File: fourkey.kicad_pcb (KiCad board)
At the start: 2 copper layers, 85.3 x 77.7 mm, 23 parts, among them K1 KEYSW, K2 KEYSW, K3 KEYSW, K4 KEYSW, SW1 RESET, U1 ProMicro

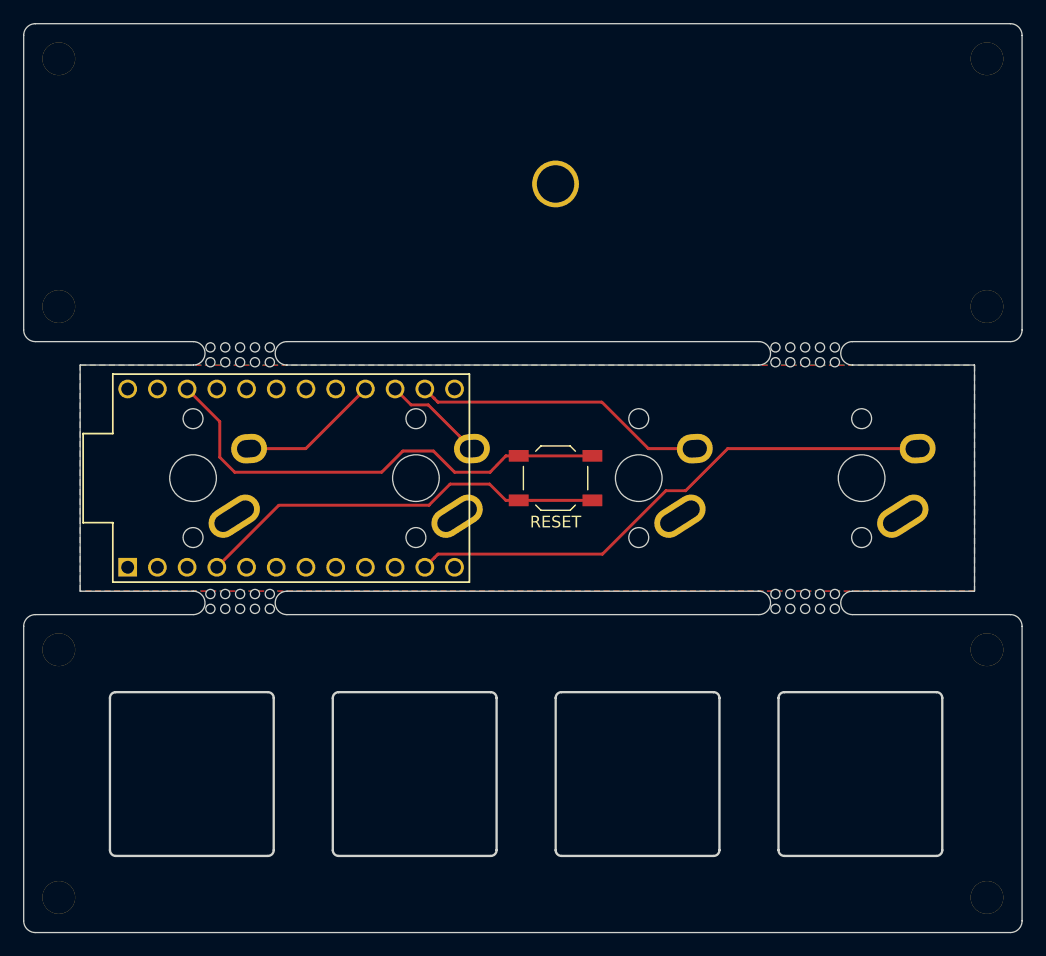
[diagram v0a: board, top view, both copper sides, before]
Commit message: change mounting holes to m2
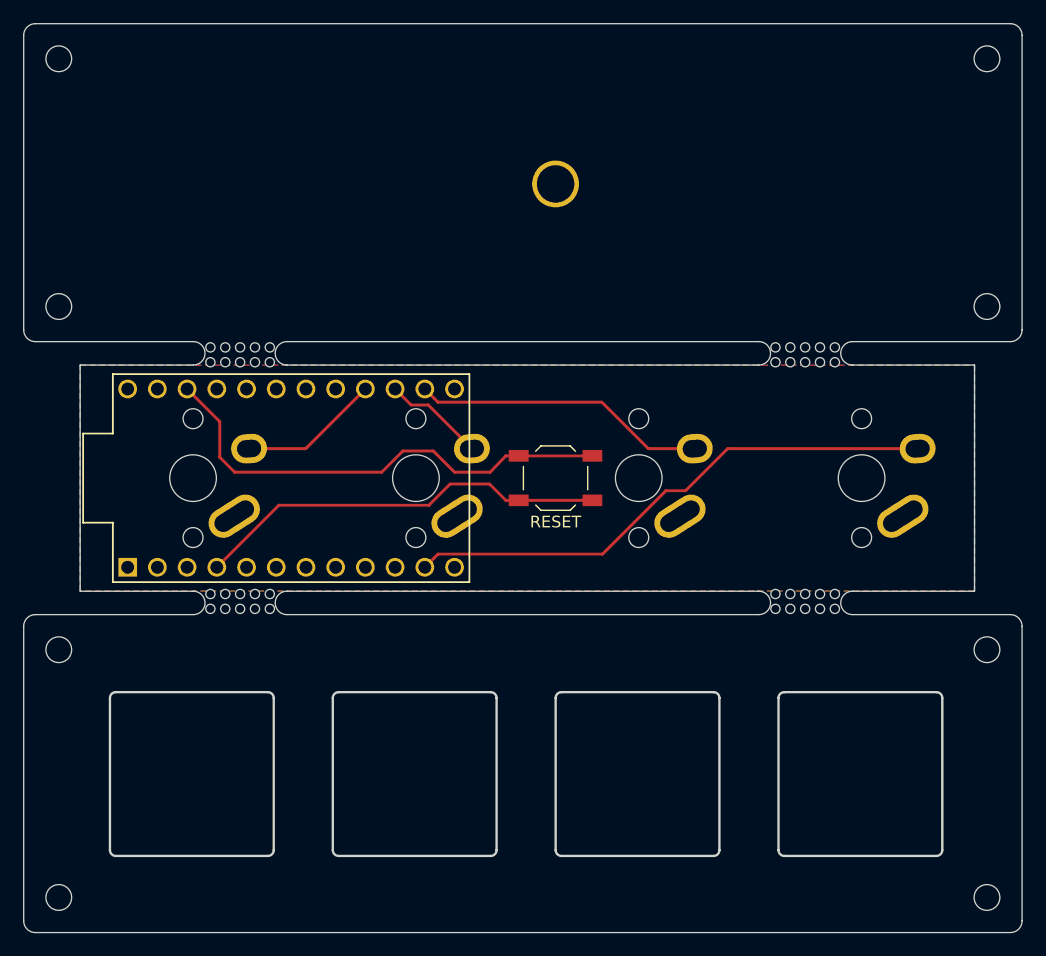
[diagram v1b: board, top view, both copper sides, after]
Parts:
- HOLE_M2.6 (x8): footprint keyboard_parts:HOLE_M2.6 -> MountingHole:MountingHole_2.2mm_M2_DIN965

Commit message: add extra screw holes
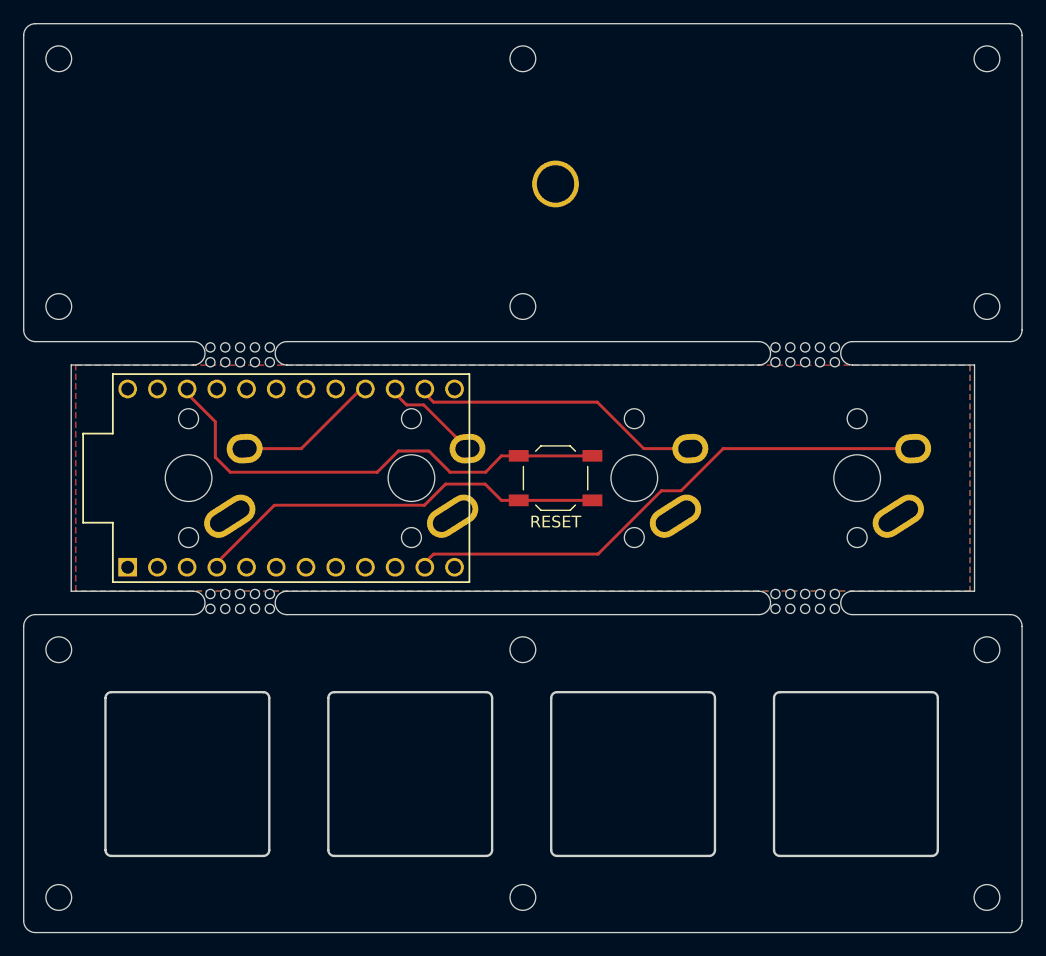
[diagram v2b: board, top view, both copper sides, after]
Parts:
- added HOLE_M2.6: VAL**, MountingHole:MountingHole_2.2mm_M2_DIN965, F.Cu at (106.2, 94.2)
- added HOLE_M2.6: VAL**, MountingHole:MountingHole_2.2mm_M2_DIN965, F.Cu at (106.2, 115.3)
- added HOLE_M2.6: VAL**, MountingHole:MountingHole_2.2mm_M2_DIN965, F.Cu at (106.2, 43.7)
- added HOLE_M2.6: VAL**, MountingHole:MountingHole_2.2mm_M2_DIN965, F.Cu at (106.2, 64.8)
- moved K1 0.38 mm to (77.6, 79.5)
- moved K2 0.38 mm to (96.6, 79.5)
- moved K3 0.38 mm to (115.7, 79.5)
- moved K4 0.38 mm to (134.7, 79.5)
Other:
- outline, holes or cut-outs redrawn

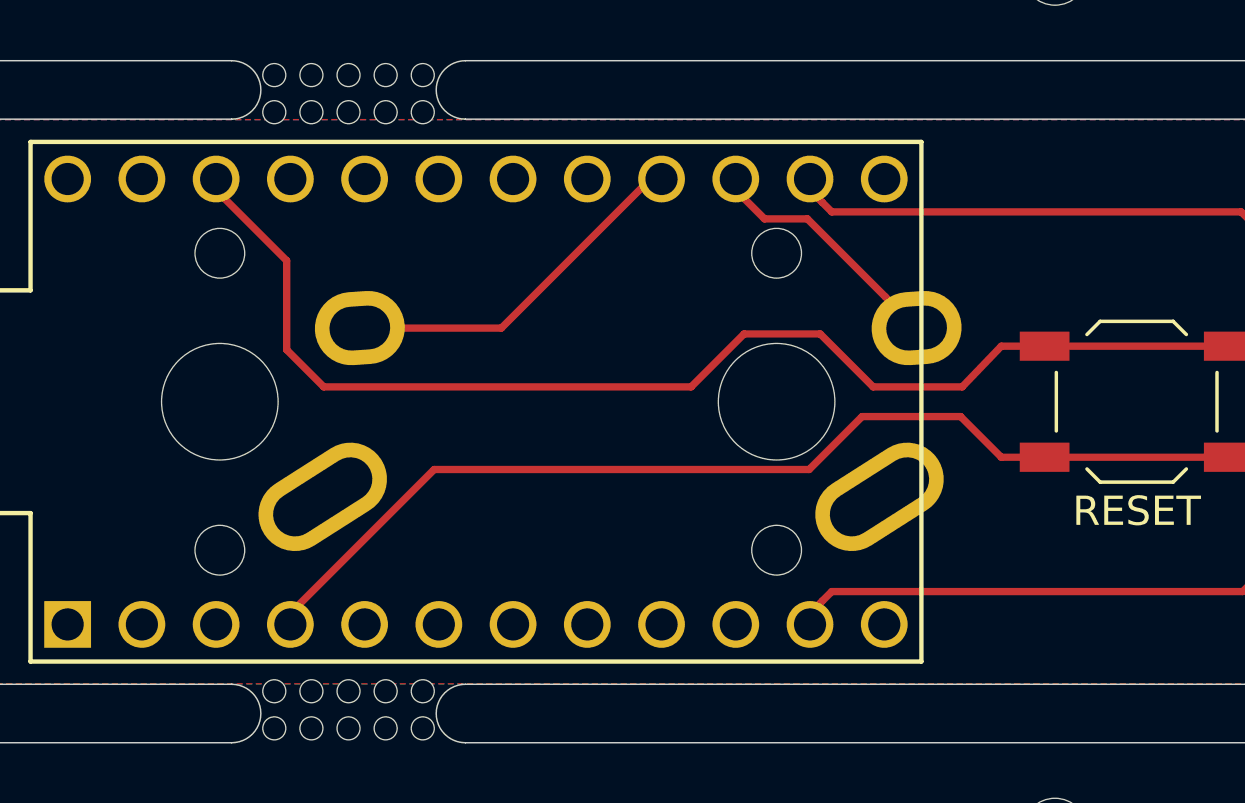
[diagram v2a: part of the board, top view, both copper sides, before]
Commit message: some trace rerouting
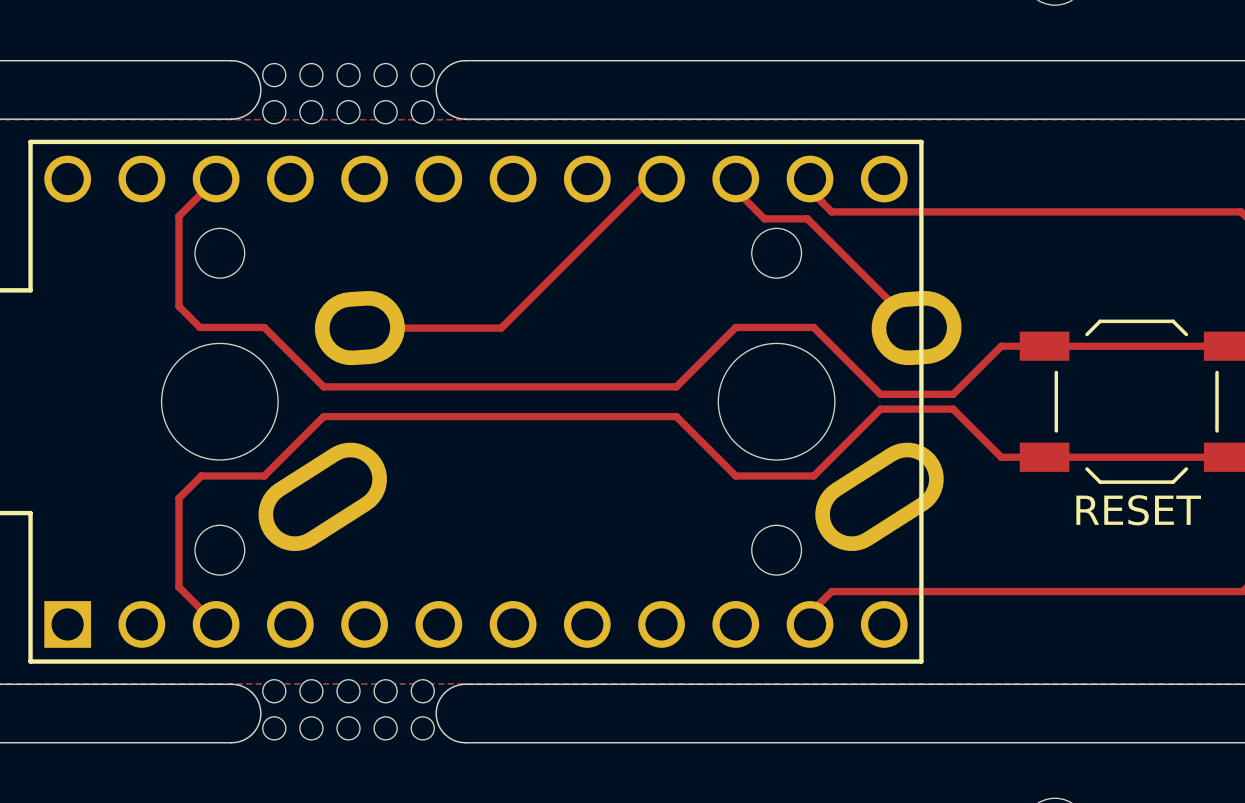
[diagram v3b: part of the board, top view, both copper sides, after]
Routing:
- net +5V: track 35.6 -> 44.0 mm
- net /Reset: track 41.5 -> 44.0 mm
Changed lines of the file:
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@@
     (thickness 1.6)
     (drawings 69)
-    (tracks 38)
+    (tracks 45)
     (zones 0)
     (modules 27)
@@
   (layers
     (0 F.Cu signal)
-    (31 B.Cu signal)
+    (31 B.Cu signal hide)
     (32 B.Adhes user)
     (33 F.Adhes user)
@@
     (38 B.Mask user)
     (39 F.Mask user)
-    (40 Dwgs.User user)
+    (40 Dwgs.User user hide)
     (41 Cmts.User user)
     (42 Eco1.User user)
@@
   (segment (start 139.537 76.982) (end 123.297 76.982) (width 0.25) (layer F.Cu) (net 7))
   (segment (start 105.435 77.602) (end 111.735 77.602) (width 0.25) (layer F.Cu) (net 9))
-  (segment (start 102.997 78.994) (end 104.335 77.602) (width 0.25) (layer F.Cu) (net 9))
   (segment (start 104.335 77.602) (end 105.435 77.602) (width 0.25) (layer F.Cu) (net 9))
-  (segment (start 98.138099 77.183099) (end 99.949 78.994) (width 0.25) (layer F.Cu) (net 9))
-  (segment (start 77.089 71.882) (end 79.883 74.676) (width 0.25) (layer F.Cu) (net 9))
-  (segment (start 93.723026 78.994) (end 95.533927 77.183099) (width 0.25) (layer F.Cu) (net 9))
-  (segment (start 81.153 78.994) (end 93.723026 78.994) (width 0.25) (layer F.Cu) (net 9))
-  (segment (start 79.883 77.724) (end 81.153 78.994) (width 0.25) (layer F.Cu) (net 9))
-  (segment (start 99.949 78.994) (end 102.997 78.994) (width 0.25) (layer F.Cu) (net 9))
-  (segment (start 95.533927 77.183099) (end 98.138099 77.183099) (width 0.25) (layer F.Cu) (net 9))
-  (segment (start 79.883 74.676) (end 79.883 77.724) (width 0.25) (layer F.Cu) (net 9))
-  (segment (start 104.335 81.402) (end 102.943 80.01) (width 0.25) (layer F.Cu) (net 10))
-  (segment (start 105.435 81.402) (end 104.335 81.402) (width 0.25) (layer F.Cu) (net 10))
-  (segment (start 102.943 80.01) (end 99.570974 80.01) (width 0.25) (layer F.Cu) (net 10))
+  (segment (start 100.203 79.248) (end 102.689 79.248) (width 0.25) (layer F.Cu) (net 9))
+  (segment (start 76.917333 76.962) (end 79.121 76.962) (width 0.25) (layer F.Cu) (net 9))
+  (segment (start 97.917 76.962) (end 100.203 79.248) (width 0.25) (layer F.Cu) (net 9))
+  (segment (start 95.25 76.962) (end 97.917 76.962) (width 0.25) (layer F.Cu) (net 9))
+  (segment (start 93.218 78.994) (end 95.25 76.962) (width 0.25) (layer F.Cu) (net 9))
+  (segment (start 77.47 71.882) (end 76.2 73.152) (width 0.25) (layer F.Cu) (net 9))
+  (segment (start 79.121 76.962) (end 81.153 78.994) (width 0.25) (layer F.Cu) (net 9))
+  (segment (start 81.153 78.994) (end 93.218 78.994) (width 0.25) (layer F.Cu) (net 9))
+  (segment (start 76.2 76.244667) (end 76.917333 76.962) (width 0.25) (layer F.Cu) (net 9))
+  (segment (start 102.689 79.248) (end 104.335 77.602) (width 0.25) (layer F.Cu) (net 9))
+  (segment (start 76.2 73.152) (end 76.2 76.244667) (width 0.25) (layer F.Cu) (net 9))
   (segment (start 106.535 81.402) (end 111.735 81.402) (width 0.25) (layer F.Cu) (net 10))
-  (segment (start 105.435 81.402) (end 106.535 81.402) (width 0.25) (layer F.Cu) (net 10))
-  (segment (start 97.760073 81.820901) (end 99.570974 80.01) (width 0.25) (layer F.Cu) (net 10))
-  (segment (start 84.930099 81.820901) (end 97.760073 81.820901) (width 0.25) (layer F.Cu) (net 10))
-  (segment (start 79.629 87.122) (end 84.930099 81.820901) (width 0.25) (layer F.Cu) (net 10))
+  (segment (start 104.335 81.402) (end 106.535 81.402) (width 0.25) (layer F.Cu) (net 10))
+  (segment (start 76.962 82.042) (end 79.121 82.042) (width 0.25) (layer F.Cu) (net 10))
+  (segment (start 76.2 82.804) (end 76.962 82.042) (width 0.25) (layer F.Cu) (net 10))
+  (segment (start 97.917 82.042) (end 100.203 79.756) (width 0.25) (layer F.Cu) (net 10))
+  (segment (start 95.25 82.042) (end 97.917 82.042) (width 0.25) (layer F.Cu) (net 10))
+  (segment (start 102.689 79.756) (end 104.335 81.402) (width 0.25) (layer F.Cu) (net 10))
+  (segment (start 81.153 80.01) (end 93.218 80.01) (width 0.25) (layer F.Cu) (net 10))
+  (segment (start 100.203 79.756) (end 102.689 79.756) (width 0.25) (layer F.Cu) (net 10))
+  (segment (start 93.218 80.01) (end 95.25 82.042) (width 0.25) (layer F.Cu) (net 10))
+  (segment (start 76.2 85.852) (end 76.2 82.804) (width 0.25) (layer F.Cu) (net 10))
+  (segment (start 79.121 82.042) (end 81.153 80.01) (width 0.25) (layer F.Cu) (net 10))
+  (segment (start 77.47 87.122) (end 76.2 85.852) (width 0.25) (layer F.Cu) (net 10))
   (zone (net 0) (net_name "") (layer F.Cu) (hatch edge 0.508)
     (connect_pads (clearance 0.508))
